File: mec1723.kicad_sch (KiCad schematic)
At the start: 0 parts

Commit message: [#103224] Add QSPI Flash section, add .ci.yml
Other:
- note added: "https://ww1.microchip.com/downloads/aemDocuments/documents/CPG/ProductDocuments/DataSheets/MEC172x-Data-Sheet-DS00003583.pdf"
- note added: "https://www.microchip.com/en-us/product/mec1723"
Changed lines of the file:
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@@
 	(generator_version "10.0")
 	(paper "A4")
+	(text "https://ww1.microchip.com/downloads/aemDocuments/documents/CPG/ProductDocuments/DataSheets/MEC172x-Data-Sheet-DS00003583.pdf"
+		(exclude_from_sim no)
+		(at 87.122 20.828 0)
+		(effects
+			(font
+				(size 1.27 1.27)
+			)
+		)
+	)
+	(text "https://www.microchip.com/en-us/product/mec1723"
+		(exclude_from_sim no)
+		(at 42.926 17.272 0)
+		(effects
+			(font
+				(size 1.27 1.27)
+			)
+		)
+	)
 )

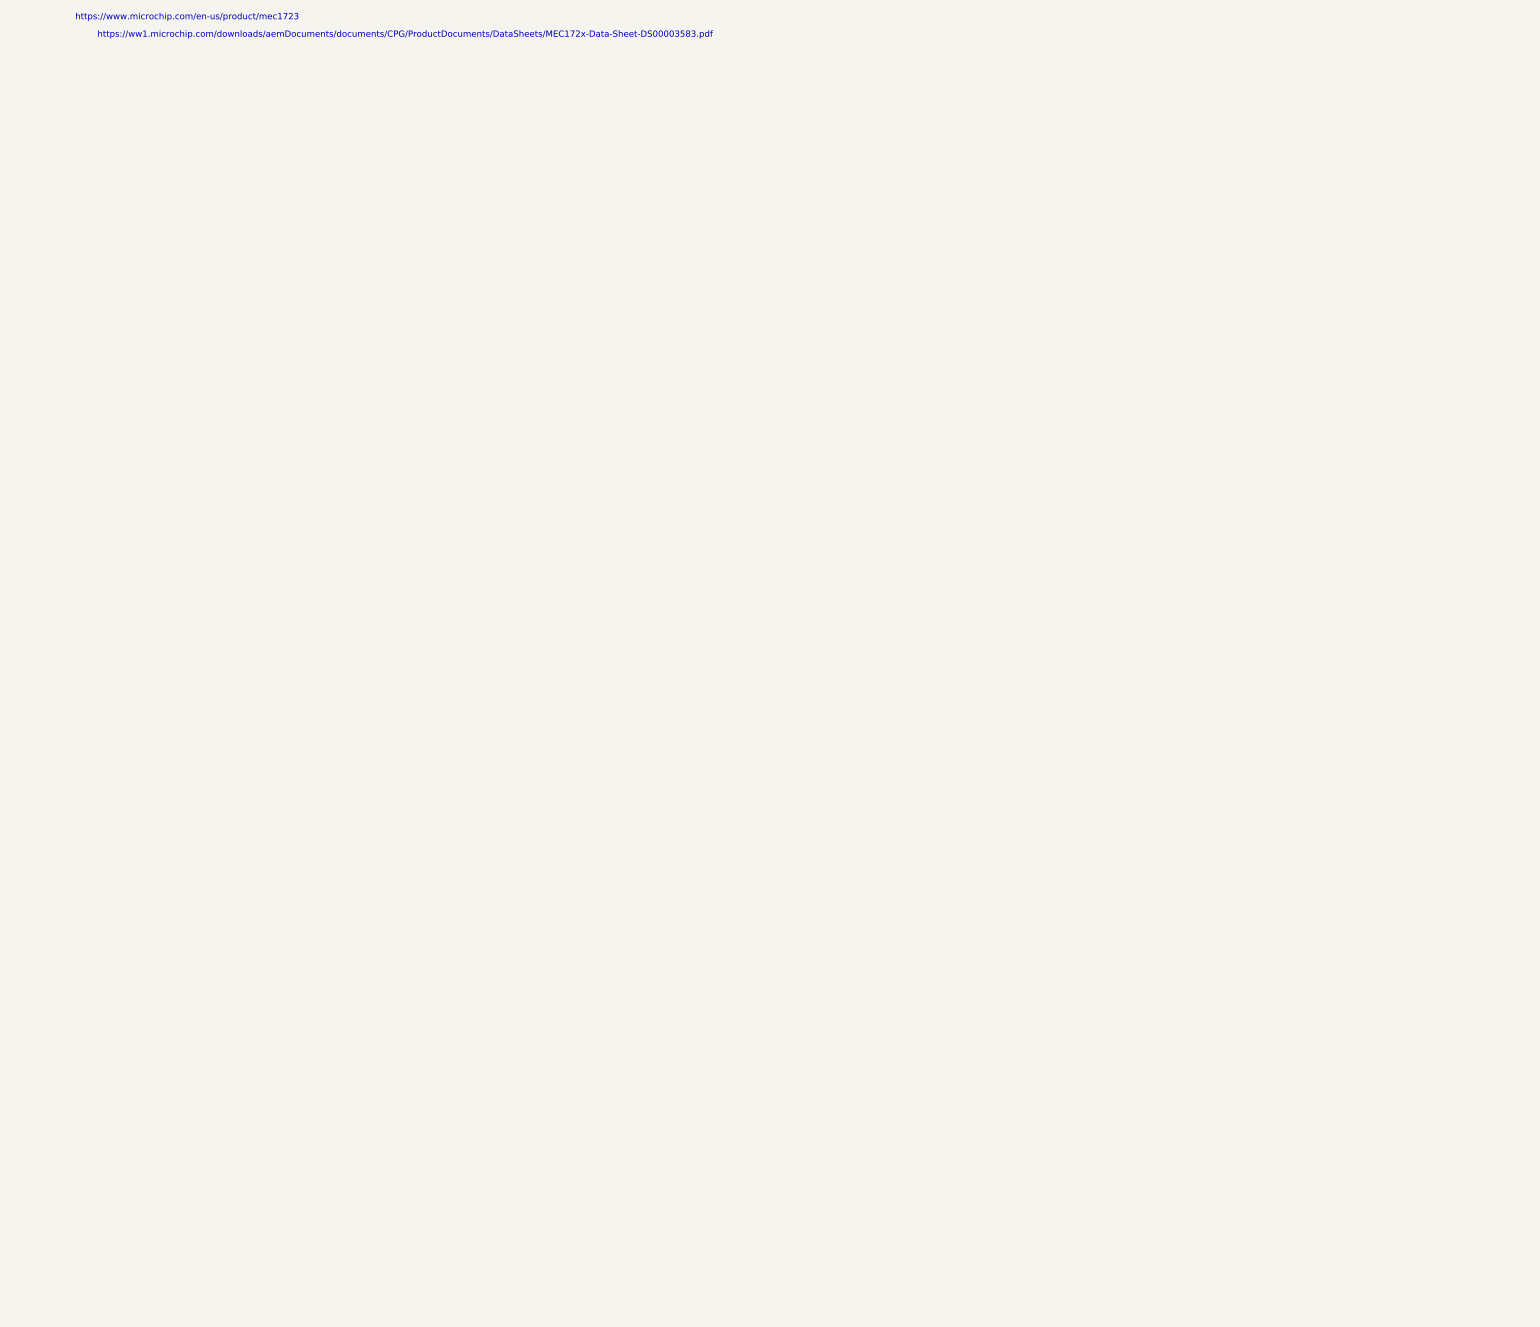
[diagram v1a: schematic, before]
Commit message: [#103224] Add MEC1723 IC, JTAG connections, eSPI connections, QSPI connections, fix typo in UART
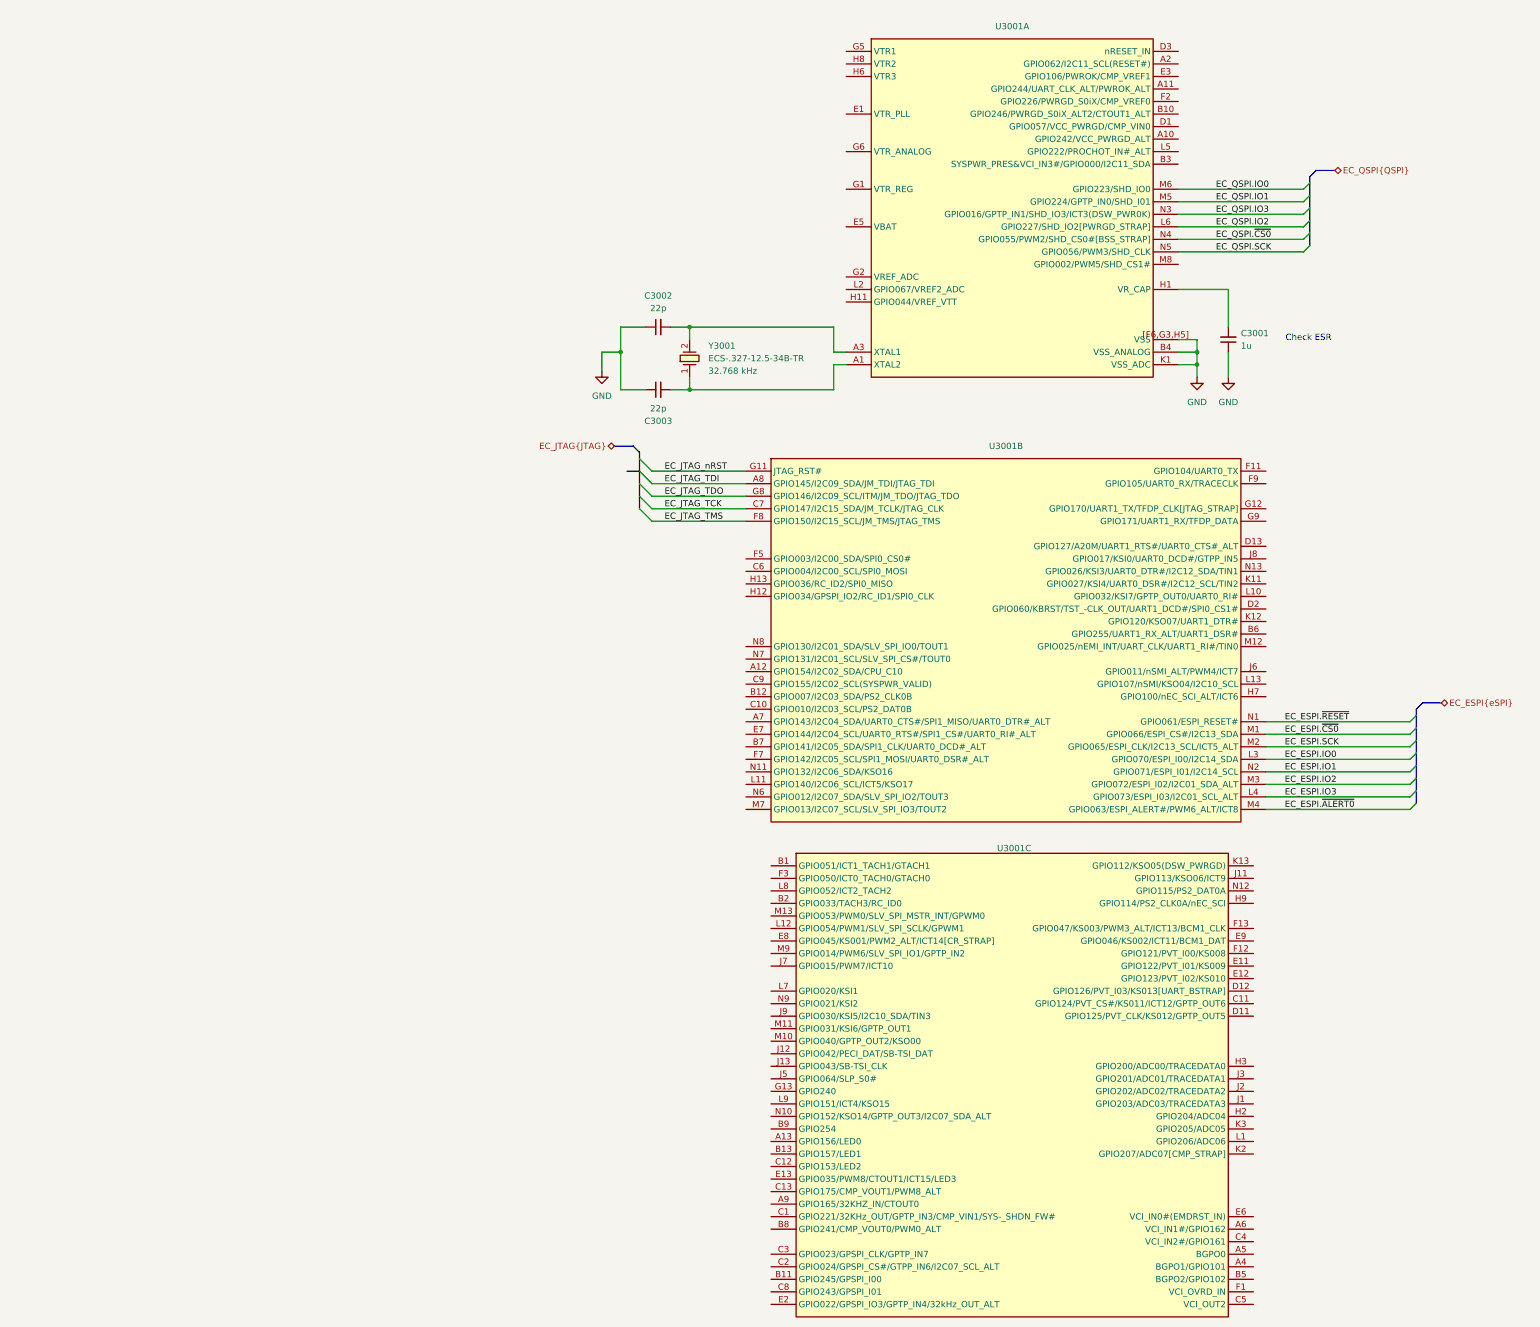
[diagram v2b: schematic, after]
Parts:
- added C3001: C_1u_6.3V_X6S_0402, antmicro-footprints:C_0402_1005Metric, symbol Antmicro Symbols:C_1u_6.3V_X6S_0402
- added C3002, C3003: C_22p_0402, antmicro-footprints:C_0402_1005Metric, symbol Antmicro Symbols:C_22p_0402
- added U3001: (no value), symbol InterfaceControllers:MEC1723N-B0-I/SZ
- added Y3001: Resonator_32.768kHz_ECX-31B, antmicro-footprints:Resonator_SMD_ECS_ECX-31B_3.2x1.5x0.9mm, symbol Antmicro Symbols:Resonator_32.768kHz_ECX-31B
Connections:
- new net: C3001.2, U3001.H1 (VR_CAP)
- new net: C3003.2, U3001.A1 (XTAL2), Y3001.1
- new net: C3002.2, U3001.A3 (XTAL1), Y3001.2
- new net EC_ESPI.IO0: U3001.L3 (GPIO070/ESPI_I00/I2C14_SDA)
- new net EC_ESPI.IO1: U3001.N2 (GPIO071/ESPI_I01/I2C14_SCL)
- new net EC_ESPI.IO2: U3001.M3 (GPIO072/ESPI_I02/I2C01_SDA_ALT)
- new net EC_ESPI.IO3: U3001.L4 (GPIO073/ESPI_I03/I2C01_SCL_ALT)
- new net EC_ESPI.SCK: U3001.M2 (GPIO065/ESPI_CLK/I2C13_SCL/ICT5_ALT)
- new net EC_ESPI.~{ALERT0}: U3001.M4 (GPIO063/ESPI_ALERT#/PWM6_ALT/ICT8)
- new net EC_ESPI.~{CS0}: U3001.M1 (GPIO066/ESPI_CS#/I2C13_SDA)
- new net EC_ESPI.~{RESET}: U3001.N1 (GPIO061/ESPI_RESET#)
- new net EC_JTAG_TCK: U3001.C7 (GPIO147/I2C15_SDA/JM_TCLK/JTAG_CLK)
- new net EC_JTAG_TDI: U3001.A8 (GPIO145/I2C09_SDA/JM_TDI/JTAG_TDI)
- new net EC_JTAG_TDO: U3001.G8 (GPIO146/I2C09_SCL/ITM/JM_TDO/JTAG_TDO)
- new net EC_JTAG_TMS: U3001.F8 (GPIO150/I2C15_SCL/JM_TMS/JTAG_TMS)
- new net EC_JTAG_nRST: U3001.G11 (JTAG_RST#)
- new net EC_QSPI.IO0: U3001.M6 (GPIO223/SHD_IO0)
- new net EC_QSPI.IO1: U3001.M5 (GPIO224/GPTP_IN0/SHD_I01)
- new net EC_QSPI.IO2: U3001.L6 (GPIO227/SHD_IO2[PWRGD_STRAP])
- new net EC_QSPI.IO3: U3001.N3 (GPIO016/GPTP_IN1/SHD_IO3/ICT3(DSW_PWR0K))
- new net EC_QSPI.SCK: U3001.N5 (GPIO056/PWM3/SHD_CLK)
- new net EC_QSPI.~{CS0}: U3001.N4 (GPIO055/PWM2/SHD_CS0#[BSS_STRAP])
- new net GND: C3001.1, C3002.1, C3003.1, U3001.B4 (VSS_ANALOG), U3001.K1 (VSS_ADC), U3001.[F6,G3,H5] (VSS)
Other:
- note added: "Check ESR"
- note removed: "https://ww1.microchip.com/downloads/aemDocuments/documents/CPG/ProductDocuments/DataSheets/MEC172x-Data-Sheet-DS00003583.pdf"
- note removed: "https://www.microchip.com/en-us/product/mec1723"

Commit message: [#103224] Add decoupling, add reset, add notes
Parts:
- added C3004, C3005, C3006, C3007, C3008, C3009, C3011: C_100n_0402, antmicro-footprints:C_0402_1005Metric, symbol Capacitors0402:C_100n_0402
- added C3010: C_1u_6.3V_X6S_0402, antmicro-footprints:C_0402_1005Metric, symbol Antmicro Symbols:C_1u_6.3V_X6S_0402
- added R3001: R_100R_0402, antmicro-footprints:R_0402_1005Metric, symbol Antmicro Symbols:R_100R_0402
- added R3002: R_10k_0402, antmicro-footprints:R_0402_1005Metric, symbol Antmicro Symbols:R_10k_0402
- added SW3001: SW_B3U-1000P_SMD, antmicro-footprints:SW_B3U-1000P_SMD, symbol Antmicro Symbols:SW_B3U-1000P_SMD
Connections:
- net GND: now also C3004.1, C3005.1, C3006.1, C3007.1, C3008.1, C3009.1, C3010.1, C3011.1, SW3001.2
- net at U3001.D3 (nRESET_IN): now also C3010.2, R3001.1, R3002.2
- net +3V3: now reaches U3001.E1 (VTR_PLL)
- net +3V3: now also U3001.G1 (VTR_REG), U3001.G5 (VTR1), U3001.G6 (VTR_ANALOG), C3004.2, C3005.2, C3006.2, C3009.2, R3002.1
- net at U3001.G2 (VREF_ADC): now also C3011.2
- net +1V8: now reaches U3001.H6 (VTR3)
- net +1V8: now also U3001.H8 (VTR2), C3007.2, C3008.2
- new net: R3001.2, SW3001.1
- no-connect marks 0 -> 1
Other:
- note added: "Add battery circuit"

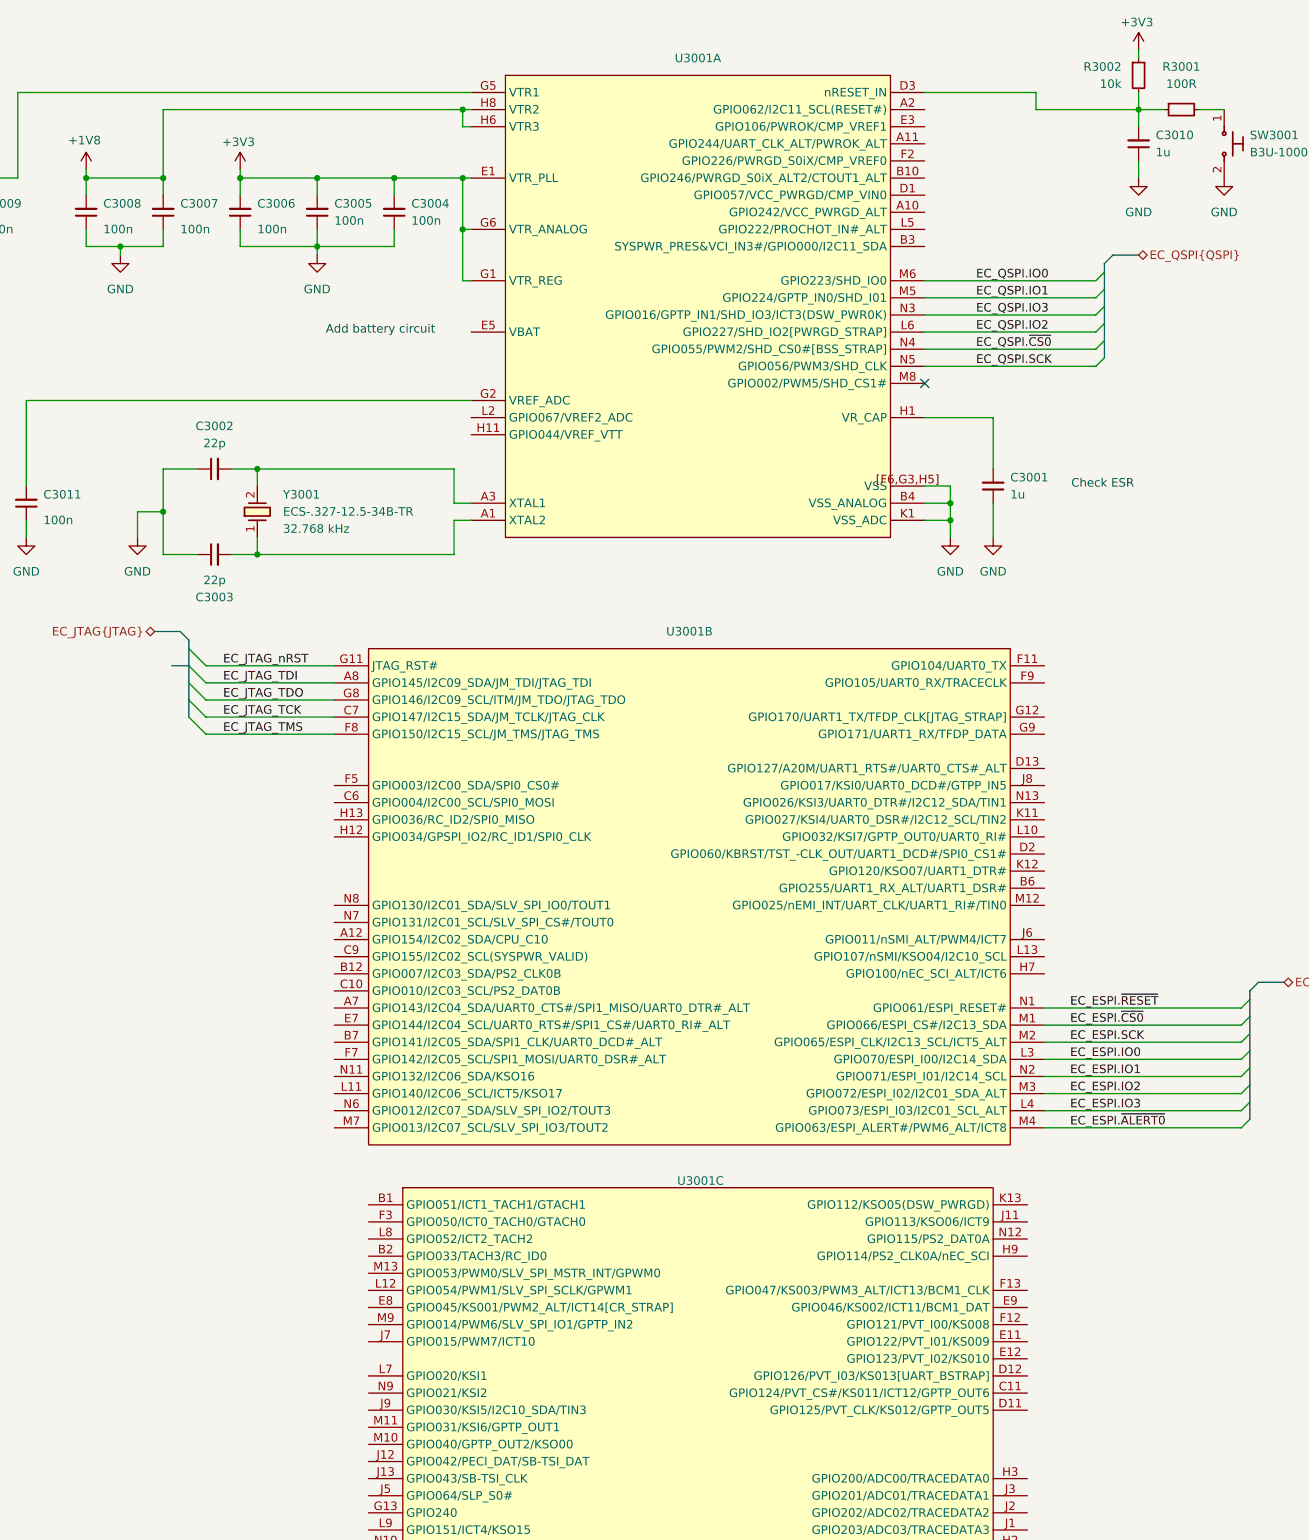
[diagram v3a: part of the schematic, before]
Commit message: [#103224] Add 7-segment display section, add battery cicruit
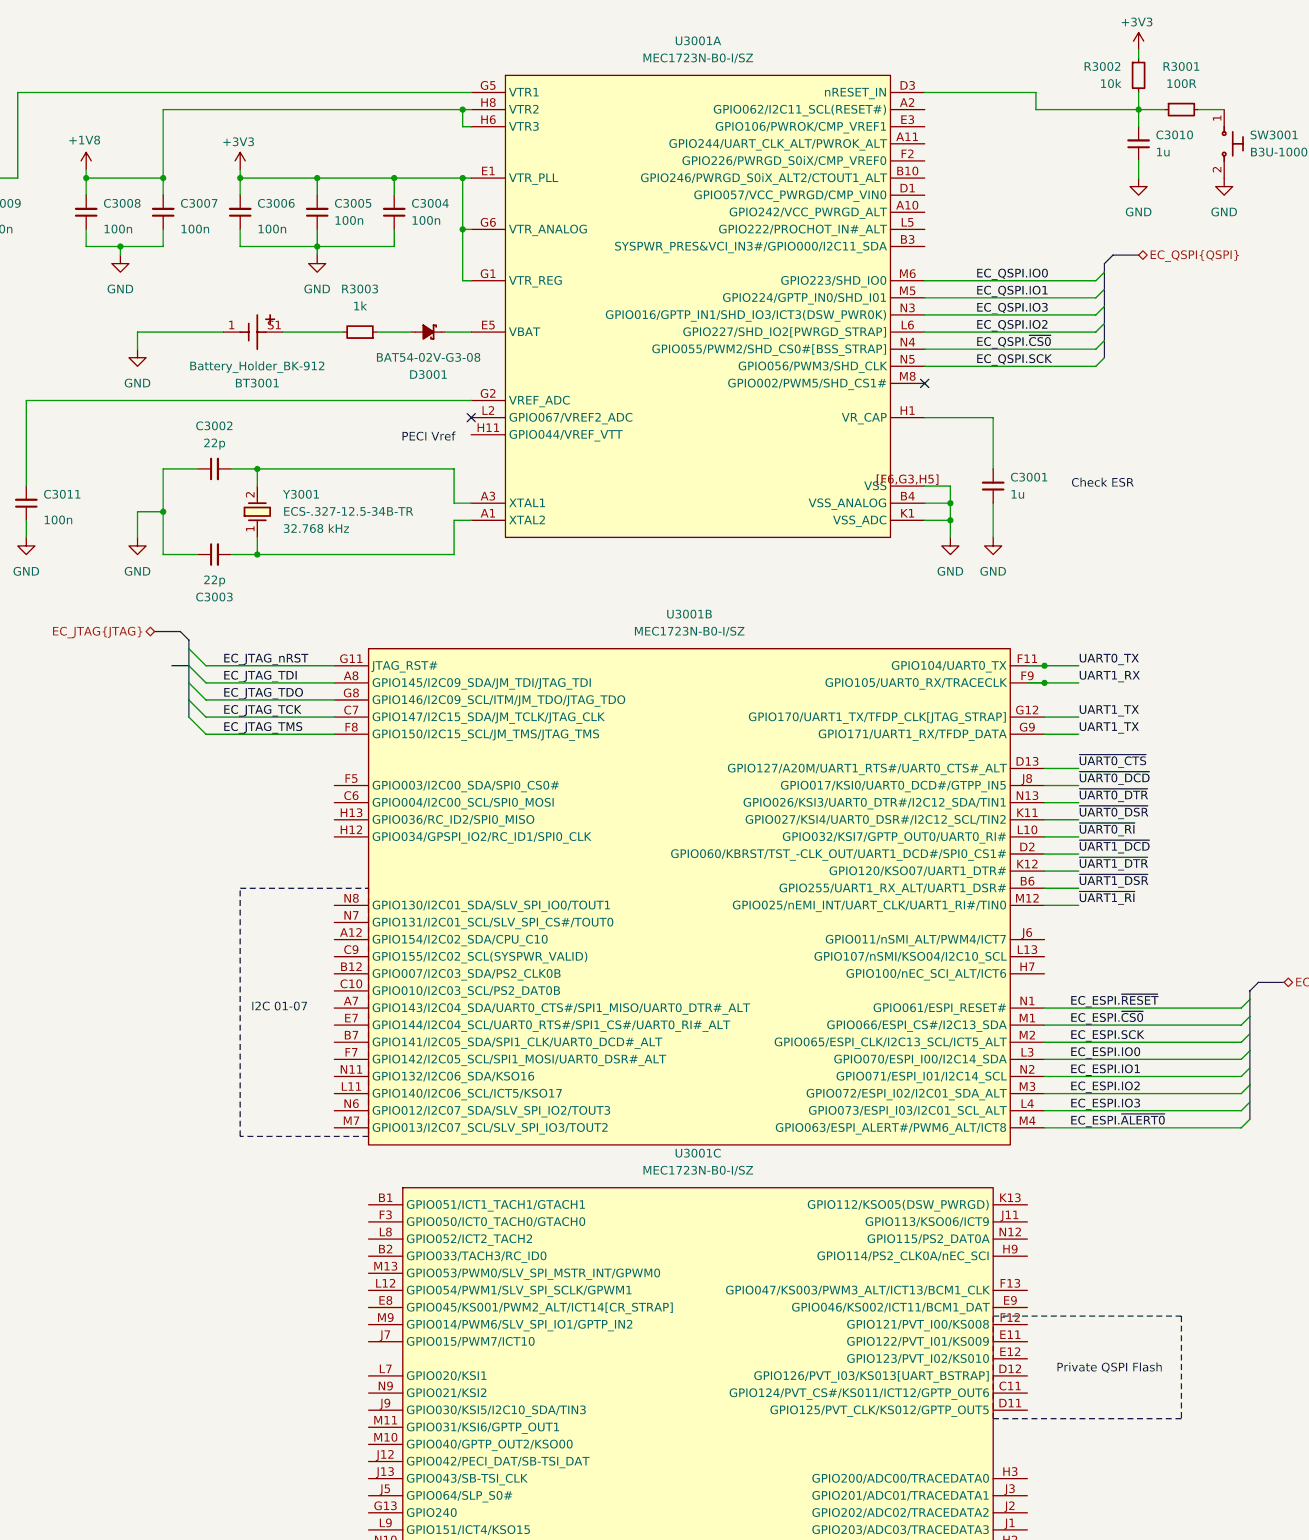
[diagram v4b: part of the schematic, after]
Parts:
- added BT3001: Battery_Holder_BK-912, antmicro-footprints:Battery_Holder_BK-912, symbol Antmicro Symbols:Battery_Holder_BK-912
- added D3001: BAT54-02V-G3-08, antmicro-footprints:SOD-523, symbol Antmicro Symbols:BAT54-02V-G3-08
- added R3003: R_1k_0402, antmicro-footprints:R_0402_1005Metric, symbol Antmicro Symbols:R_1k_0402
- U3001: value (none) -> MEC1723N-B0-I/SZ; footprint (none) -> antmicro-footprints:BGA-169-144_9x9mm_Layout13x13_P0.7mm; Author (none) -> Antmicro; License (none) -> Apache-2.0; MPN (none) -> MEC1723N-B0-I/SZ; Manufacturer (none) -> Microchip Technology
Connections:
- net GND: now also BT3001.1 (GND)
- net at U3001.E5 (VBAT): now also D3001.1 (C)
- net ~{UART1_DSR}: now reaches U3001.B6 (GPIO255/UART1_RX_ALT/UART1_DSR#)
- net ~{UART0_CTS}: now reaches U3001.D13 (GPIO127/A20M/UART1_RTS#/UART0_CTS#_ALT)
- net ~{UART1_DCD}: now reaches U3001.D2 (GPIO060/KBRST/TST_-CLK_OUT/UART1_DCD#/SPI0_CS1#)
- net UART0_TX: now reaches U3001.F11 (GPIO104/UART0_TX)
- net UART1_RX: now reaches U3001.F9 (GPIO105/UART0_RX/TRACECLK)
- net UART1_TX: now reaches U3001.G12 (GPIO170/UART1_TX/TFDP_CLK[JTAG_STRAP])
- net UART1_TX: now also U3001.G9 (GPIO171/UART1_RX/TFDP_DATA)
- net ~{UART0_DCD}: now reaches U3001.J8 (GPIO017/KSI0/UART0_DCD#/GTPP_IN5)
- net ~{UART0_DSR}: now reaches U3001.K11 (GPIO027/KSI4/UART0_DSR#/I2C12_SCL/TIN2)
- net ~{UART1_DTR}: now reaches U3001.K12 (GPIO120/KSO07/UART1_DTR#)
- net ~{UART0_RI}: now reaches U3001.L10 (GPIO032/KSI7/GPTP_OUT0/UART0_RI#)
- net ~{UART1_RI}: now reaches U3001.M12 (GPIO025/nEMI_INT/UART_CLK/UART1_RI#/TIN0)
- net ~{UART0_DTR}: now reaches U3001.N13 (GPIO026/KSI3/UART0_DTR#/I2C12_SDA/TIN1)
- new net: D3001.2 (A), R3003.1
- new net: BT3001.S1 (V_BAT), BT3001.S2 (V_BAT), R3003.2
- no-connect marks 1 -> 2
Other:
- note added: "I2C 01-07"
- note added: "PECI Vref"
- note added: "Private QSPI Flash"
- note removed: "Add battery circuit"
